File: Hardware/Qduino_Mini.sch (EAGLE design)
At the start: 38 parts, among them J1 LiPo, Q1 PFET, U1 ATMEGA32U41:1-LESS_PASTE, U2 MCP73831, U3 MAX17048, U4 AP2112K-3.3TRG-1, U5 MIGHTYQ-L-SILK, Y1 8MHZ

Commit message: Fixed issues
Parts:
- D3: PROD_ID DIO-12986 -> DIO-12985
- Q1: value PFET -> ZXMP6A13FTA
- R1, R2: value 330 -> 1KΩ
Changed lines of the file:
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@@
 <part name="P+6" library="SFE Aesthetics" deviceset="VCC" device=""/>
 <part name="GND20" library="SparkFun" deviceset="GND" device=""/>
-<part name="Q1" library="SparkFun-DiscreteSemi" deviceset="MOSFET-PCHANNEL" device="" value="PFET"/>
+<part name="Q1" library="SparkFun-DiscreteSemi" deviceset="MOSFET-PCHANNEL" device="" value="ZXMP6A13FTA"/>
 <part name="GND21" library="SparkFun" deviceset="GND" device=""/>
 <part name="GND1" library="SparkFun" deviceset="GND" device=""/>
@@
 <part name="SUPPLY2" library="SparkFun-Aesthetics" deviceset="VCC" device=""/>
 <part name="D3" library="Testing" deviceset="0.13_RGB_LED" device="PLCC">
-<attribute name="PROD_ID" value="DIO-12986"/>
+<attribute name="PROD_ID" value="DIO-12985"/>
 </part>
 <part name="SUPPLY1" library="SparkFun-Aesthetics" deviceset="VCC" device=""/>
-<part name="R1" library="SparkFun-Passives" deviceset="RESISTOR-ARRAY" device="0603-ARV" value="330">
+<part name="R1" library="SparkFun-Passives" deviceset="RESISTOR-ARRAY" device="0603-ARV" value="1KΩ">
 <attribute name="PROD_ID" value="RES-12985"/>
 </part>
-<part name="R2" library="SparkFun-Passives" deviceset="RESISTOR-ARRAY" device="0603-ARV" value="330">
+<part name="R2" library="SparkFun-Passives" deviceset="RESISTOR-ARRAY" device="0603-ARV" value="1KΩ">
 <attribute name="PROD_ID" value="RES-12985"/>
 </part>
@@
 <instance part="P+6" gate="1" x="147.32" y="10.16"/>
 <instance part="GND20" gate="1" x="147.32" y="-7.62"/>
-<instance part="Q1" gate="G$1" x="137.16" y="50.8" smashed="yes" rot="MR180">
-<attribute name="NAME" x="138.43" y="48.006" size="1.778" layer="95" rot="MR180"/>
-</instance>
+<instance part="Q1" gate="G$1" x="137.16" y="50.8" rot="MR180"/>
 <instance part="GND21" gate="1" x="116.84" y="33.02"/>
 <instance part="GND1" gate="1" x="111.76" y="-7.62"/>
@@
 <instance part="D1" gate="G$1" x="127" y="63.5" smashed="yes">
 <attribute name="NAME" x="129.54" y="63.9826" size="1.778" layer="95"/>
+<attribute name="VALUE" x="124.714" y="59.9186" size="1.778" layer="96"/>
 </instance>
 <instance part="U5" gate="G$1" x="78.74" y="0"/>

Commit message: Switched LEDs to those in the live library vs testing
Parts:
- D2: device Testing:0.13_RGB_LEDPLCC -> SparkFun-LED:0.13_RGB_LEDPLCC
- D3: device Testing:0.13_RGB_LEDPLCC -> SparkFun-LED:0.13_RGB_LEDPLCC; PROD_ID DIO-12985 -> (none)
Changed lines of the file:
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@@
 <?xml version="1.0" encoding="utf-8"?>
 <!DOCTYPE eagle SYSTEM "eagle.dtd">
-<eagle version="7.3.0">
+<eagle version="7.2.0">
 <drawing>
 <settings>
@@
 <part name="LOGO1" library="SparkFun-Aesthetics" deviceset="OSHW-LOGO" device="S"/>
 <part name="LOGO2" library="SparkFun-Aesthetics" deviceset="SFE_LOGO_FLAME" device=".1_INCH"/>
-<part name="D2" library="Testing" deviceset="0.13_RGB_LED" device="PLCC">
+<part name="D2" library="SparkFun-LED" deviceset="0.13_RGB_LED" device="PLCC">
 <attribute name="PROD_ID" value="DIO-12986"/>
 </part>
 <part name="SUPPLY2" library="SparkFun-Aesthetics" deviceset="VCC" device=""/>
-<part name="D3" library="Testing" deviceset="0.13_RGB_LED" device="PLCC">
-<attribute name="PROD_ID" value="DIO-12985"/>
-</part>
+<part name="D3" library="SparkFun-LED" deviceset="0.13_RGB_LED" device="PLCC"/>
 <part name="SUPPLY1" library="SparkFun-Aesthetics" deviceset="VCC" device=""/>
 <part name="R1" library="SparkFun-Passives" deviceset="RESISTOR-ARRAY" device="0603-ARV" value="1KΩ">

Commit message: Updated PROD_ID for Vreg to new part
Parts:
- U4: PROD_ID IC-12550 -> VREG-12457
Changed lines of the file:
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@@
 <?xml version="1.0" encoding="utf-8"?>
 <!DOCTYPE eagle SYSTEM "eagle.dtd">
-<eagle version="7.2.0">
+<eagle version="7.3.1">
 <drawing>
 <settings>
@@
 <part name="GND15" library="SparkFun-Aesthetics" deviceset="GND" device=""/>
 <part name="U4" library="SparkFun-PowerIC" deviceset="LDO-TPS78233" device="" value="AP2112K-3.3TRG-1">
-<attribute name="PROD_ID" value="IC-12550"/>
+<attribute name="PROD_ID" value="VREG-12457"/>
 </part>
 <part name="C7" library="SparkFun-Capacitors" deviceset="2.2UF-10V-20%(0603)" device="" value="2.2uF"/>

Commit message: Added 10KΩ pull-up to reset line
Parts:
- added R8: 10K, SparkFun-Resistors:10KOHM-1/10W-1%(0603)0603
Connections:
- net !RST: now also R8.1
- net VCC: now also R8.2
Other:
- moved on the sheet: JP3, JP4, U1

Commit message: RXLED & TXLED were swapped. Noted errata.
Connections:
- net RXLED: now also R1B.1, U1.PB0(SS); no longer R1C.1, U1.PD5
- net TXLED: now also R1C.1, U1.PD5; no longer R1B.1, U1.PB0(SS)
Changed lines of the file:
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@@
 </segment>
 </net>
-<net name="TXLED" class="0">
+<net name="RXLED" class="0">
 <segment>
 <wire x1="-33.02" y1="43.18" x2="-35.56" y2="43.18" width="0.1524" layer="91"/>
@@
 </segment>
 </net>
-<net name="RXLED" class="0">
+<net name="TXLED" class="0">
 <segment>
 <wire x1="-35.56" y1="30.48" x2="-33.02" y2="30.48" width="0.1524" layer="91"/>

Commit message: Added notes to schematic & updated board manager files
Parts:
- D4: value GREEN -> POWER
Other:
- note added: "GREEN LED LIT WHEN CHARGING"
- note added: "STAT"
- note added: "USER"
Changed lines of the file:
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@@
 <?xml version="1.0" encoding="utf-8"?>
 <!DOCTYPE eagle SYSTEM "eagle.dtd">
-<eagle version="7.3.1">
+<eagle version="7.2.0">
 <drawing>
 <settings>
@@
 <part name="GND2" library="SFE Aesthetics" deviceset="GND" device=""/>
 <part name="GND3" library="SFE Aesthetics" deviceset="GND" device=""/>
-<part name="D4" library="SparkFun-LED" deviceset="LED-GREEN" device="0603" value="GREEN">
+<part name="D4" library="SparkFun-LED" deviceset="LED-GREEN" device="0603" value="POWER">
 <attribute name="PROD_ID" value="DIO-00821"/>
 </part>
@@
 <text x="62.23" y="-43.18" size="2.54" layer="94" ratio="5">Revised by: Brent Wilkins</text>
 <text x="132.08" y="83.82" size="1.778" layer="97" font="vector" align="center">I2C ADDRESS = 0x36</text>
+<text x="53.34" y="60.96" size="1.778" layer="97" font="vector">USER</text>
+<text x="27.94" y="60.96" size="1.778" layer="97" font="vector">STAT</text>
+<text x="15.24" y="22.86" size="1.27" layer="97" font="vector">GREEN LED LIT WHEN CHARGING</text>
 </plain>
 <instances>

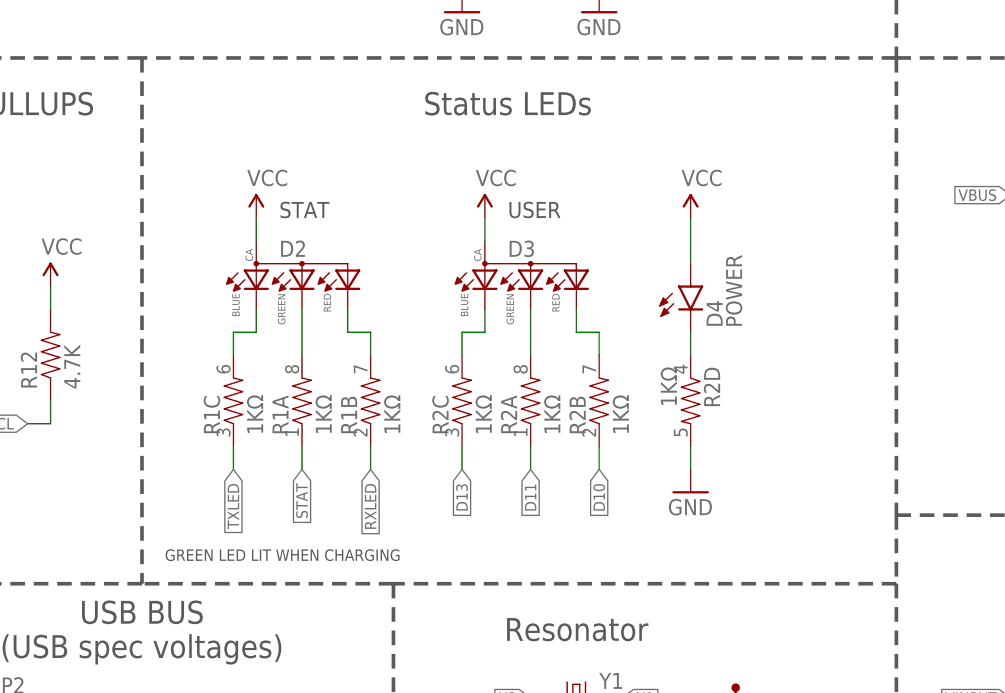
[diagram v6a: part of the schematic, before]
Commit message: Fixed MISO D# & powered USB LEDs directly from USB
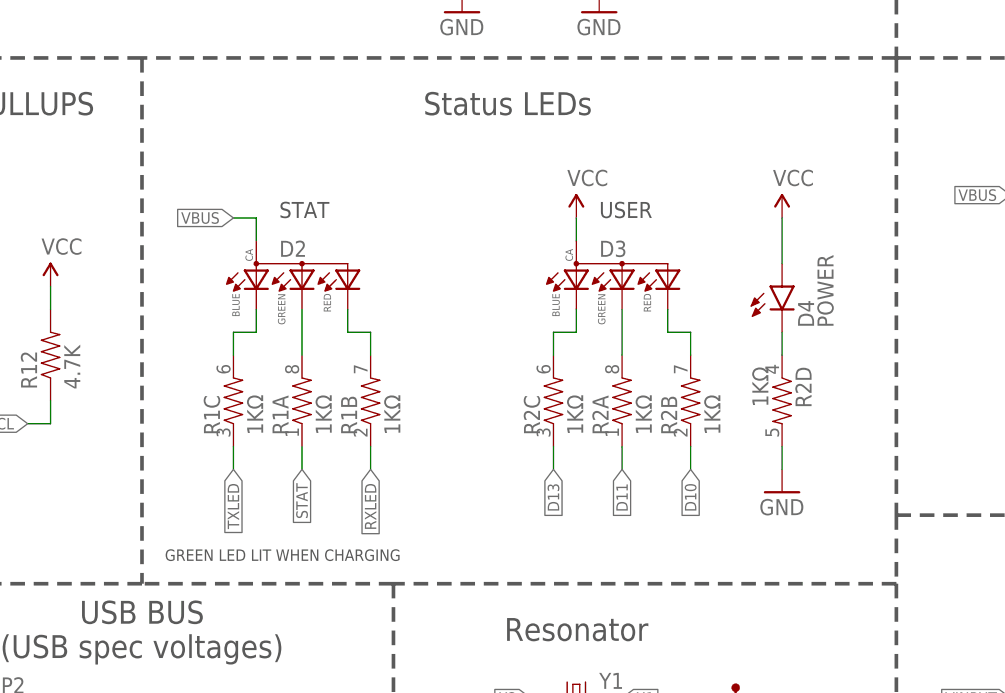
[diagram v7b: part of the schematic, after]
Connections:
- net VBUS: now also D2.ANODE
- net VCC: no longer D2.ANODE
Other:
- moved on the sheet: D3, D4, R2A, R2B, R2C, R2D
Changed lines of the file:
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@@
 <?xml version="1.0" encoding="utf-8"?>
 <!DOCTYPE eagle SYSTEM "eagle.dtd">
-<eagle version="7.2.0">
+<eagle version="7.3.0">
 <drawing>
 <settings>
@@
 <attribute name="PROD_ID" value="DIO-12986"/>
 </part>
-<part name="SUPPLY2" library="SparkFun-Aesthetics" deviceset="VCC" device=""/>
 <part name="D3" library="SparkFun-LED" deviceset="0.13_RGB_LED" device="PLCC"/>
 <part name="SUPPLY1" library="SparkFun-Aesthetics" deviceset="VCC" device=""/>
@@
 <text x="62.23" y="-43.18" size="2.54" layer="94" ratio="5">Revised by: Brent Wilkins</text>
 <text x="132.08" y="83.82" size="1.778" layer="97" font="vector" align="center">I2C ADDRESS = 0x36</text>
-<text x="53.34" y="60.96" size="1.778" layer="97" font="vector">USER</text>
+<text x="63.5" y="60.96" size="1.778" layer="97" font="vector">USER</text>
 <text x="27.94" y="60.96" size="1.778" layer="97" font="vector">STAT</text>
 <text x="15.24" y="22.86" size="1.27" layer="97" font="vector">GREEN LED LIT WHEN CHARGING</text>
@@
 <instance part="GND2" gate="1" x="-5.08" y="-40.64"/>
 <instance part="GND3" gate="1" x="10.16" y="-40.64"/>
-<instance part="D4" gate="G$1" x="73.66" y="53.34">
-<attribute name="PROD_ID" x="73.66" y="53.34" size="1.27" layer="96" display="off"/>
-</instance>
-<instance part="P+4" gate="1" x="73.66" y="60.96"/>
-<instance part="GND6" gate="1" x="73.66" y="30.48"/>
+<instance part="D4" gate="G$1" x="83.82" y="53.34">
+<attribute name="PROD_ID" x="83.82" y="53.34" size="1.27" layer="96" display="off"/>
+</instance>
+<instance part="P+4" gate="1" x="83.82" y="60.96"/>
+<instance part="GND6" gate="1" x="83.82" y="30.48"/>
 <instance part="GND5" gate="1" x="45.72" y="-40.64"/>
 <instance part="GND14" gate="1" x="73.66" y="96.52"/>
@@
 <attribute name="PROD_ID" x="30.48" y="53.34" size="1.778" layer="96" display="off"/>
 </instance>
-<instance part="SUPPLY2" gate="G$1" x="25.4" y="60.96"/>
-<instance part="D3" gate="G$1" x="55.88" y="53.34">
-<attribute name="PROD_ID" x="55.88" y="53.34" size="1.778" layer="96" display="off"/>
-</instance>
-<instance part="SUPPLY1" gate="G$1" x="50.8" y="60.96"/>
+<instance part="D3" gate="G$1" x="66.04" y="53.34">
+<attribute name="PROD_ID" x="66.04" y="53.34" size="1.778" layer="96" display="off"/>
+</instance>
+<instance part="SUPPLY1" gate="G$1" x="60.96" y="60.96"/>
 <instance part="R1" gate="A" x="30.48" y="40.64" rot="R90"/>
 <instance part="R1" gate="B" x="38.1" y="40.64" rot="R90"/>
@@
 <attribute name="PROD_ID" x="22.86" y="40.64" size="1.778" layer="96" rot="R90" display="off"/>
 </instance>
-<instance part="R2" gate="A" x="55.88" y="40.64" rot="R90"/>
-<instance part="R2" gate="B" x="63.5" y="40.64" rot="R90"/>
-<instance part="R2" gate="C" x="48.26" y="40.64" rot="R90">
-<attribute name="PROD_ID" x="48.26" y="40.64" size="1.778" layer="96" rot="R90" display="off"/>
-</instance>
-<instance part="R2" gate="D" x="73.66" y="40.64" rot="R270"/>
+<instance part="R2" gate="A" x="66.04" y="40.64" rot="R90"/>
+<instance part="R2" gate="B" x="73.66" y="40.64" rot="R90"/>
+<instance part="R2" gate="C" x="58.42" y="40.64" rot="R90">
+<attribute name="PROD_ID" x="58.42" y="40.64" size="1.778" layer="96" rot="R90" display="off"/>
+</instance>
+<instance part="R2" gate="D" x="83.82" y="40.64" rot="R270"/>
 <instance part="JP3" gate="G$1" x="-50.8" y="-12.7">
 <attribute name="PROD_ID" x="-50.8" y="-12.7" size="1.778" layer="96" display="off"/>
@@
 <pinref part="GND6" gate="1" pin="GND"/>
 <pinref part="R2" gate="D" pin="2"/>
-<wire x1="73.66" y1="35.56" x2="73.66" y2="33.02" width="0.1524" layer="91"/>
+<wire x1="83.82" y1="35.56" x2="83.82" y2="33.02" width="0.1524" layer="91"/>
 </segment>
 <segment>
@@
 <segment>
 <pinref part="R2" gate="B" pin="1"/>
-<wire x1="63.5" y1="35.56" x2="63.5" y2="33.02" width="0.1524" layer="91"/>
-<label x="63.5" y="33.02" size="1.27" layer="95" rot="R270" xref="yes"/>
+<wire x1="73.66" y1="35.56" x2="73.66" y2="33.02" width="0.1524" layer="91"/>
+<label x="73.66" y="33.02" size="1.27" layer="95" rot="R270" xref="yes"/>
 </segment>
 </net>
@@
 <pinref part="D4" gate="G$1" pin="A"/>
 <pinref part="P+4" gate="1" pin="VCC"/>
-<wire x1="73.66" y1="60.96" x2="73.66" y2="55.88" width="0.1524" layer="91"/>
+<wire x1="83.82" y1="60.96" x2="83.82" y2="55.88" width="0.1524" layer="91"/>
 </segment>
 <segment>
@@
 </segment>
 <segment>
-<pinref part="D2" gate="G$1" pin="ANODE"/>
-<wire x1="25.4" y1="58.42" x2="25.4" y2="60.96" width="0.1524" layer="91"/>
-<pinref part="SUPPLY2" gate="G$1" pin="VCC"/>
-</segment>
-<segment>
 <pinref part="D3" gate="G$1" pin="ANODE"/>
-<wire x1="50.8" y1="58.42" x2="50.8" y2="60.96" width="0.1524" layer="91"/>
+<wire x1="60.96" y1="58.42" x2="60.96" y2="60.96" width="0.1524" layer="91"/>
 <pinref part="SUPPLY1" gate="G$1" pin="VCC"/>
 </segment>
@@
 <pinref part="JP4" gate="G$1" pin="8"/>
 </segment>
+<segment>
+<wire x1="22.86" y1="60.96" x2="25.4" y2="60.96" width="0.1524" layer="91"/>
+<pinref part="D2" gate="G$1" pin="ANODE"/>
+<wire x1="25.4" y1="58.42" x2="25.4" y2="60.96" width="0.1524" layer="91"/>
+<label x="22.86" y="60.96" size="1.27" layer="95" rot="R180" xref="yes"/>
+</segment>
 </net>
 <net name="!ALRT" class="0">
@@
 <segment>
 <pinref part="R2" gate="A" pin="1"/>
-<wire x1="55.88" y1="35.56" x2="55.88" y2="33.02" width="0.1524" layer="91"/>
-<label x="55.88" y="33.02" size="1.27" layer="95" rot="R270" xref="yes"/>
+<wire x1="66.04" y1="35.56" x2="66.04" y2="33.02" width="0.1524" layer="91"/>
+<label x="66.04" y="33.02" size="1.27" layer="95" rot="R270" xref="yes"/>
 </segment>
 </net>
@@
 <segment>
 <pinref part="R2" gate="C" pin="1"/>
-<wire x1="48.26" y1="35.56" x2="48.26" y2="33.02" width="0.1524" layer="91"/>
-<label x="48.26" y="33.02" size="1.27" layer="95" rot="R270" xref="yes"/>
+<wire x1="58.42" y1="35.56" x2="58.42" y2="33.02" width="0.1524" layer="91"/>
+<label x="58.42" y="33.02" size="1.27" layer="95" rot="R270" xref="yes"/>
 </segment>
 </net>
@@
 <pinref part="D3" gate="G$1" pin="RED"/>
 <pinref part="R2" gate="B" pin="2"/>
-<wire x1="60.96" y1="50.8" x2="60.96" y2="48.26" width="0.1524" layer="91"/>
-<wire x1="60.96" y1="48.26" x2="63.5" y2="48.26" width="0.1524" layer="91"/>
-<wire x1="63.5" y1="48.26" x2="63.5" y2="45.72" width="0.1524" layer="91"/>
+<wire x1="71.12" y1="50.8" x2="71.12" y2="48.26" width="0.1524" layer="91"/>
+<wire x1="71.12" y1="48.26" x2="73.66" y2="48.26" width="0.1524" layer="91"/>
+<wire x1="73.66" y1="48.26" x2="73.66" y2="45.72" width="0.1524" layer="91"/>
 </segment>
 </net>
@@
 <pinref part="D4" gate="G$1" pin="C"/>
 <pinref part="R2" gate="D" pin="1"/>
-<wire x1="73.66" y1="45.72" x2="73.66" y2="48.26" width="0.1524" layer="91"/>
+<wire x1="83.82" y1="45.72" x2="83.82" y2="48.26" width="0.1524" layer="91"/>
 </segment>
 </net>
@@
 <pinref part="D3" gate="G$1" pin="BLUE"/>
 <pinref part="R2" gate="C" pin="2"/>
-<wire x1="50.8" y1="50.8" x2="50.8" y2="48.26" width="0.1524" layer="91"/>
-<wire x1="50.8" y1="48.26" x2="48.26" y2="48.26" width="0.1524" layer="91"/>
-<wire x1="48.26" y1="48.26" x2="48.26" y2="45.72" width="0.1524" layer="91"/>
+<wire x1="60.96" y1="50.8" x2="60.96" y2="48.26" width="0.1524" layer="91"/>
+<wire x1="60.96" y1="48.26" x2="58.42" y2="48.26" width="0.1524" layer="91"/>
+<wire x1="58.42" y1="48.26" x2="58.42" y2="45.72" width="0.1524" layer="91"/>
 </segment>
 </net>
@@
 <pinref part="D3" gate="G$1" pin="GREEN"/>
 <pinref part="R2" gate="A" pin="2"/>
-<wire x1="55.88" y1="50.8" x2="55.88" y2="45.72" width="0.1524" layer="91"/>
-</segment>
-</net>
+<wire x1="66.04" y1="50.8" x2="66.04" y2="45.72" width="0.1524" layer="91"/>
+</segment>
+</net>
